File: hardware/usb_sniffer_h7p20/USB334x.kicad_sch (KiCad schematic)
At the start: 20 parts, among them J2 USB_C_Receptacle_USB2.0_16P, J3 USB_A, U2 LM2903A-VR, U3 LM2903A-VR, U4 LM2903A-VR, U5 USB3343

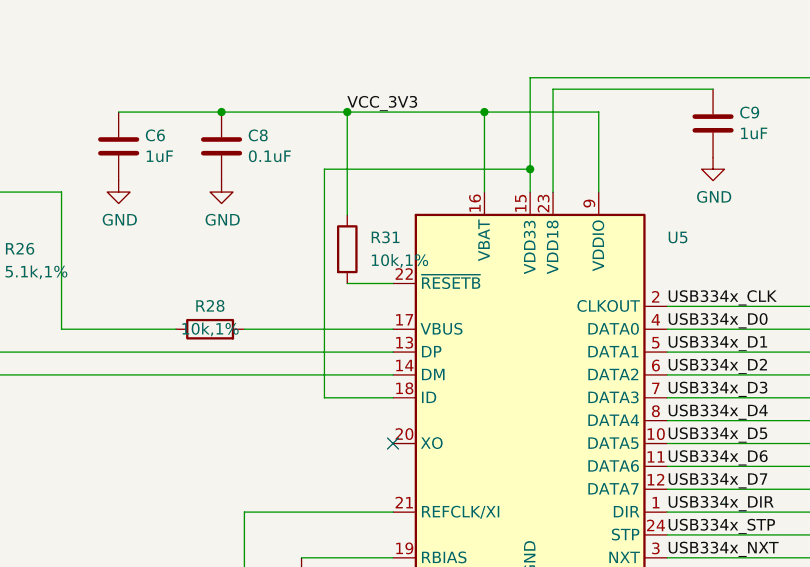
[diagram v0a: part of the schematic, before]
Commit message: [usb_sniffer_h7p20] USB3343兼容CH132F，作相关调整
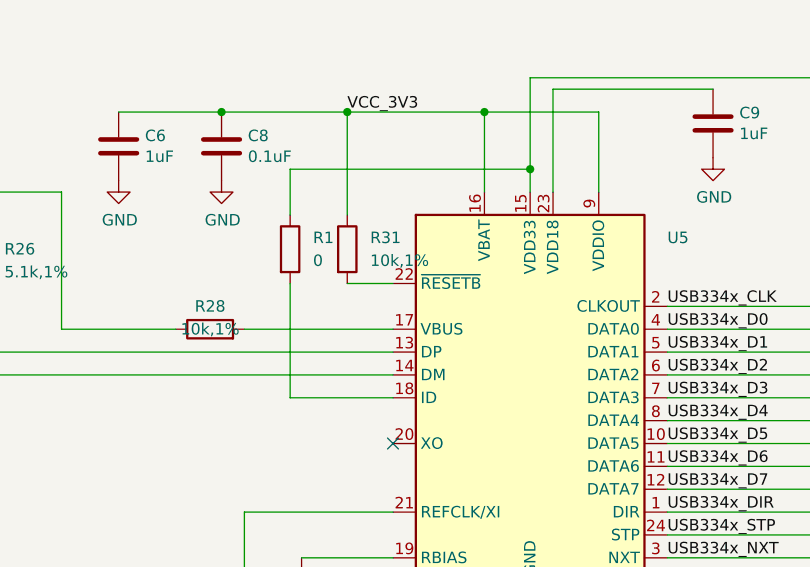
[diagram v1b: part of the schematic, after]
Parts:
- added R1: 0, Resistor_SMD:R_0402_1005Metric, symbol Device:R
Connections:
- net at C10.2, U5.15 (VDD33): now also R1.1; no longer U5.18 (ID)
- new net: R1.2, U5.18 (ID)
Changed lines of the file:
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@@
     (stroke (width 0) (type default))
   )
-  (wire (pts (xy 175.26 76.2) (xy 182.88 76.2))
+  (wire (pts (xy 171.45 76.2) (xy 182.88 76.2))
     (stroke (width 0) (type default))
   )
@@
     (stroke (width 0) (type default))
   )
-  (wire (pts (xy 175.26 50.8) (xy 198.12 50.8))
+  (wire (pts (xy 171.45 50.8) (xy 198.12 50.8))
     (stroke (width 0) (type default))
   )
@@
     (stroke (width 0) (type default))
   )
-  (wire (pts (xy 175.26 50.8) (xy 175.26 76.2))
+  (wire (pts (xy 171.45 50.8) (xy 171.45 55.88))
     (stroke (width 0) (type default))
   )
@@
   )
   (wire (pts (xy 116.84 68.58) (xy 125.73 68.58))
+    (stroke (width 0) (type default))
+  )
+  (wire (pts (xy 171.45 63.5) (xy 171.45 76.2))
     (stroke (width 0) (type default))
   )
@@
         )
       )
+    )
+  )
+  (symbol (lib_id "Device:R") (at 171.45 59.69 0) (unit 1)
+    (in_bom yes) (on_board yes) (dnp no) (fields_autoplaced)
+    (property "Reference" "R1" (at 173.99 58.42 0)
+      (effects (font (size 1.27 1.27)) (justify left))
+    )
+    (property "Value" "0" (at 173.99 60.96 0)
+      (effects (font (size 1.27 1.27)) (justify left))
+    )
+    (property "Footprint" "Resistor_SMD:R_0402_1005Metric" (at 169.672 59.69 90)
+      (effects (font (size 1.27 1.27)) hide)
+    )
+    (property "Datasheet" "~" (at 171.45 59.69 0)
+      (effects (font (size 1.27 1.27)) hide)
+    )
+    (pin "2")
+    (pin "1")
+    (instances
+      (project "usb_sniffer_h7p20"
+        (path "/5a8287a8-9f7a-4e60-a3bf-19c1227b20fe/f5b7f82e-a1df-40b6-9f59-134d2c724739"
+          (reference "R1") (unit 1)
+        )
+      )

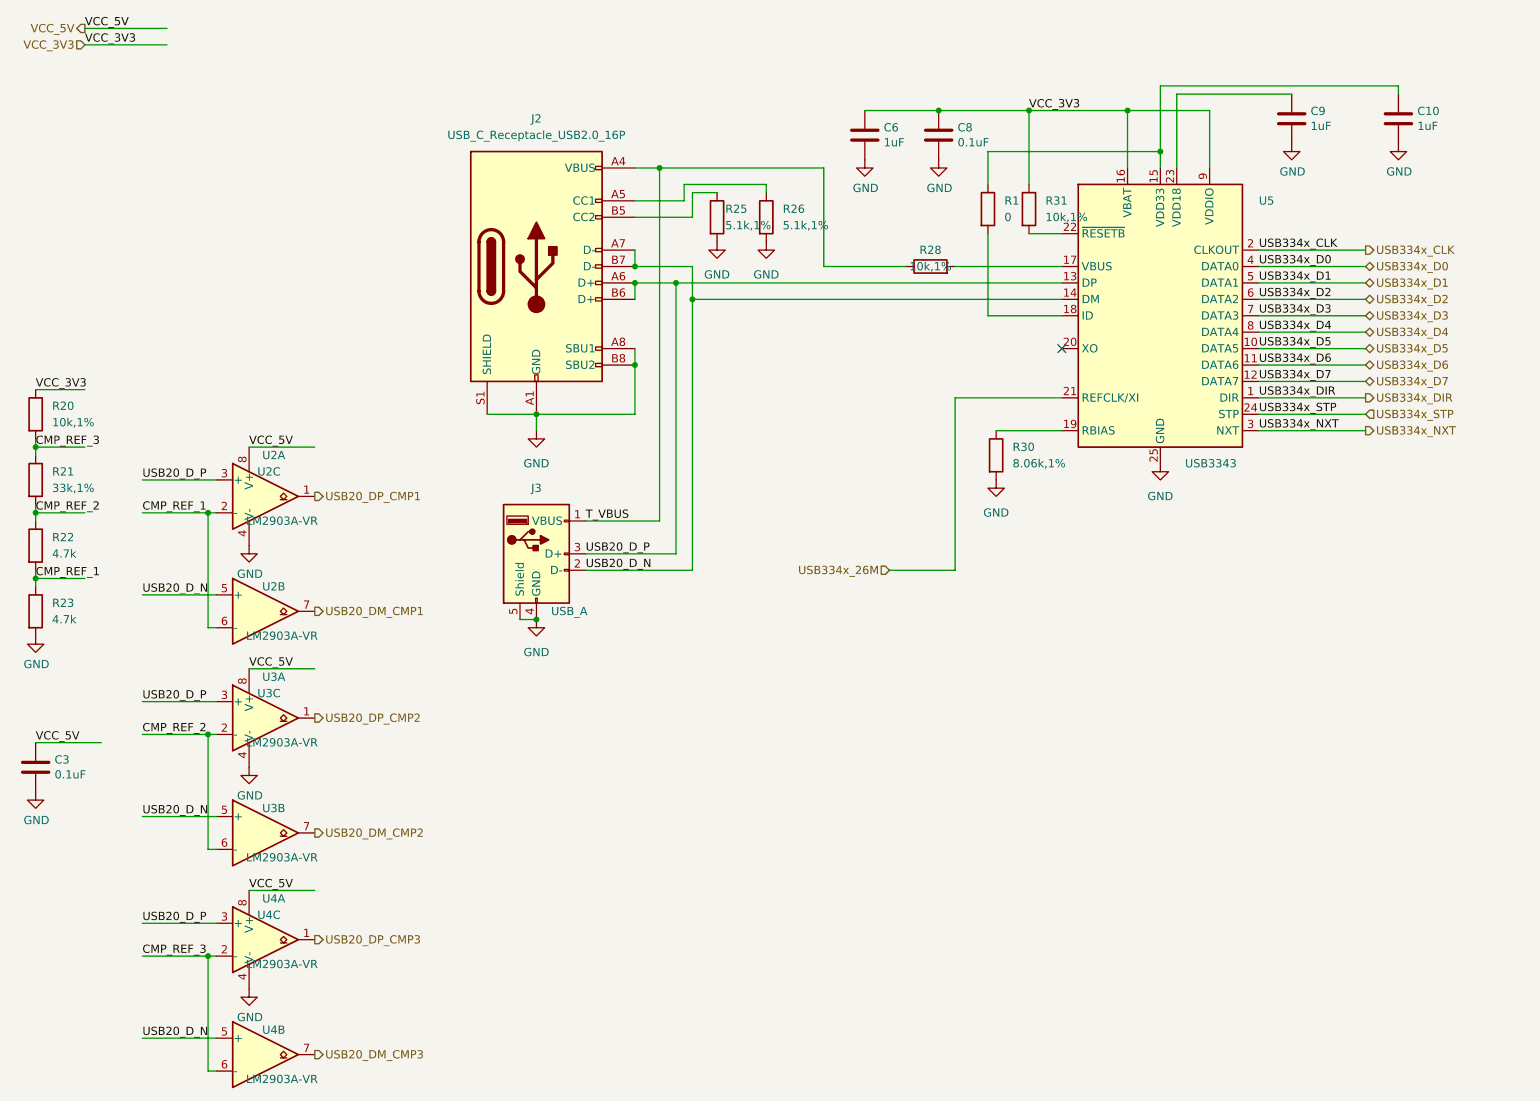
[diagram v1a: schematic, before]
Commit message: 将USB3343替换为CH132C，ULPI时钟由FPGA产生
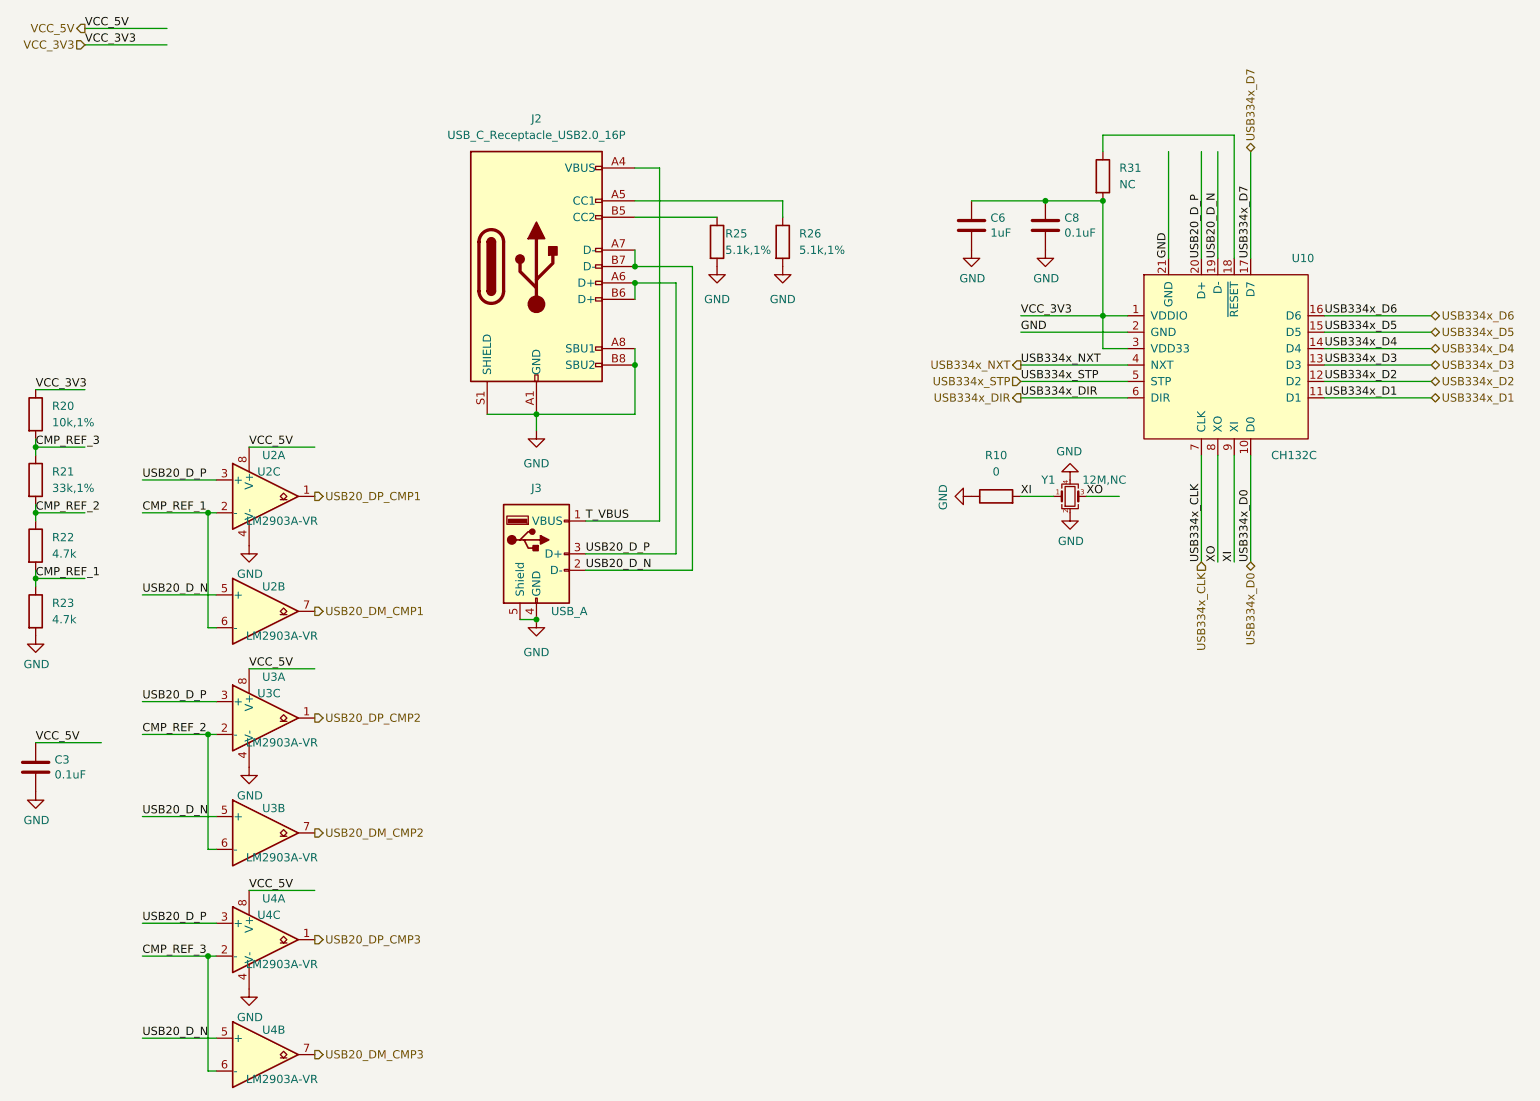
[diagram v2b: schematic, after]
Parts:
- removed C10, C9: 1uF, Capacitor_SMD:C_0402_1005Metric, symbol Device:C
- removed R1: 0, Resistor_SMD:R_0402_1005Metric, symbol Device:R
- removed R28: 10k,1%, Resistor_SMD:R_0402_1005Metric, symbol Device:R
- removed R30: 8.06k,1%, Resistor_SMD:R_0402_1005Metric, symbol Device:R
- removed U5: USB3343, Package_DFN_QFN:QFN-24-1EP_4x4mm_P0.5mm_EP2.6x2.6mm, symbol Interface_USB:USB3343
- added R10: 0, Resistor_SMD:R_0402_1005Metric, symbol Device:R
- added U10: CH132C, symbol vllogic_chip:CH132C
- added Y1: 12M,NC, vllogic:OSC_3225, symbol Device:Crystal_GND24_Small
- R31: value 10k,1% -> NC
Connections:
- net GND: now also R10.1, U10.2 (GND), U10.21 (GND), Y1.2, Y1.4
- net USB20_D_N: now also U10.19 (D-)
- net USB20_D_P: now also U10.20 (D+)
- net USB334x_CLK: now also U10.7 (CLK)
- net USB334x_D0: now also U10.10 (D0)
- net USB334x_D1: now also U10.11 (D1)
- net USB334x_D2: now also U10.12 (D2)
- net USB334x_D3: now also U10.13 (D3)
- net USB334x_D4: now also U10.14 (D4)
- net USB334x_D5: now also U10.15 (D5)
- net USB334x_D6: now also U10.16 (D6)
- net USB334x_D7: now also U10.17 (D7)
- net USB334x_DIR: now also U10.6 (DIR)
- net USB334x_NXT: now also U10.4 (NXT)
- net USB334x_STP: now also U10.5 (STP)
- net VCC_3V3: now also R31.2, U10.1 (VDDIO), U10.3 (VDD33); no longer R31.1
- new net: R31.1, U10.18 (~{RESET})
- new net XI: R10.2, U10.9 (XI), Y1.1
- new net XO: U10.8 (XO), Y1.3
- no-connect marks 1 -> 0
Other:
- moved on the sheet: C6, C8, R25, R26, R31

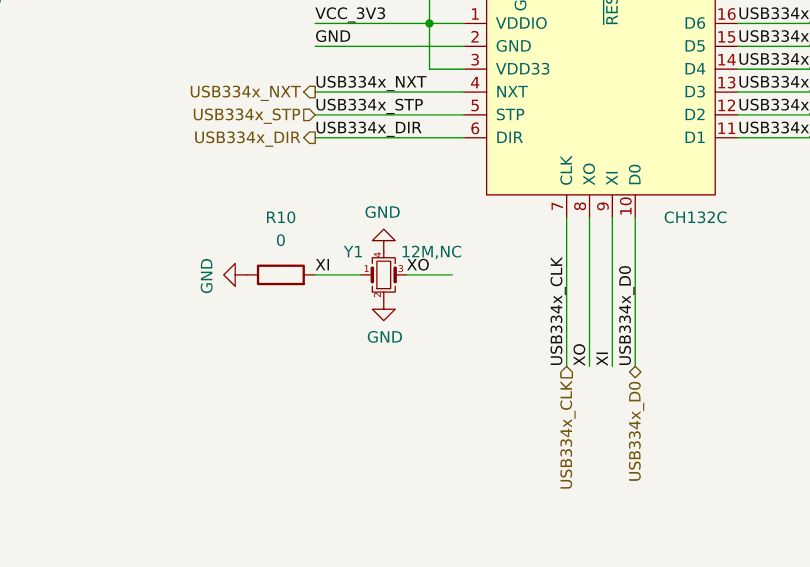
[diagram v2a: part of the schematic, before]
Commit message: [usb_sniffer_h7p20] 适配铝合金外壳、更换CH132C
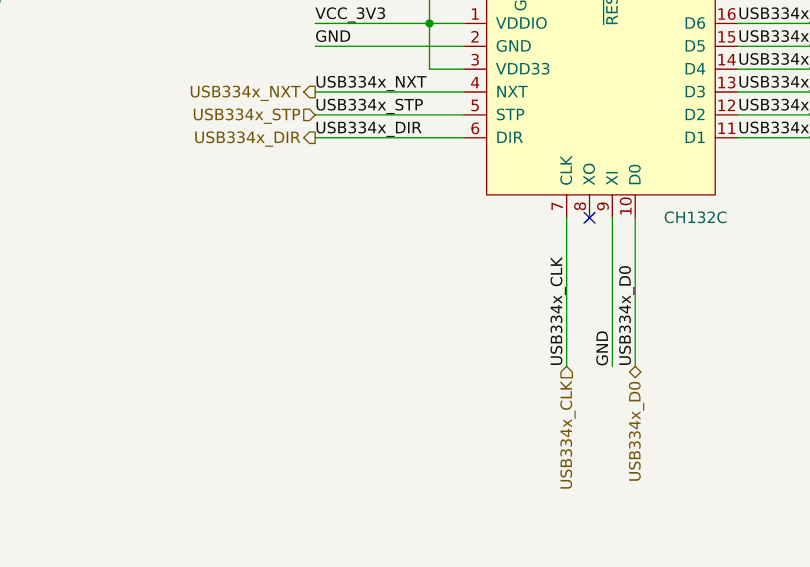
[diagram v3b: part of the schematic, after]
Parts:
- removed R10: 0, Resistor_SMD:R_0402_1005Metric, symbol Device:R
- removed Y1: 12M,NC, vllogic:OSC_3225, symbol Device:Crystal_GND24_Small
- U10: footprint (none) -> vllogic:QFN20C_2x2
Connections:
- net XI is gone; now on net GND: U10.9 (XI)
- net XO: no longer names the net of U10.8 (XO)
- no-connect marks 0 -> 1
